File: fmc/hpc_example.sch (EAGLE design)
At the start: 4 parts

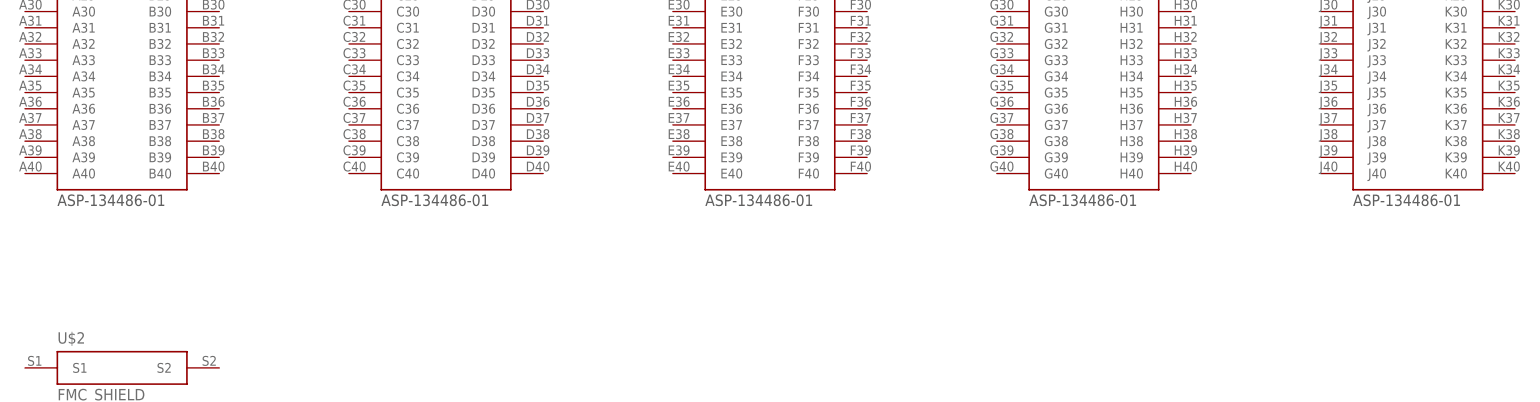
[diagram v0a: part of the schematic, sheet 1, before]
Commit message: added fmc lpc connector
updated naming
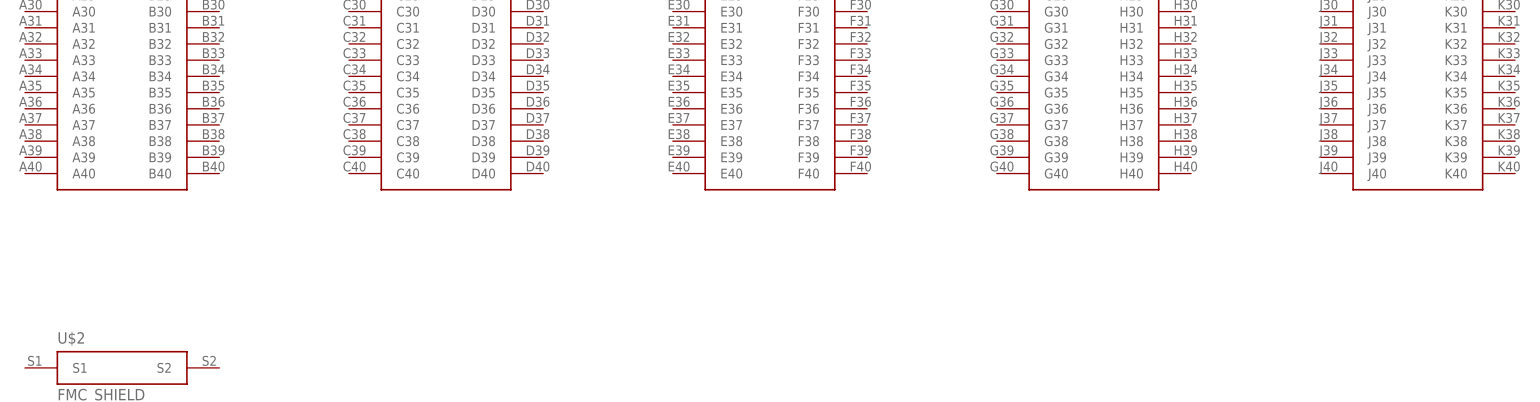
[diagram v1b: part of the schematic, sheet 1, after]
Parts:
- U$1: value FMC_HPC_M -> APS_HPC_M; device flipbit_fmc:FMC_HPC_M -> flipbit_fmc:APS_HPC_M
- U$3: value FMC_HPC_F -> APS_HPC_F; device flipbit_fmc:FMC_HPC_F -> flipbit_fmc:APS_HPC_F
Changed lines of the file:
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@@
 </classes>
 <parts>
-<part name="U$1" library="flipbit_fmc" deviceset="FMC_HPC_M" device=""/>
+<part name="U$1" library="flipbit_fmc" deviceset="APS_HPC_M" device=""/>
 <part name="U$2" library="flipbit_fmc" deviceset="XILINX_FMC_MOUNT_CS" device=""/>
-<part name="U$3" library="flipbit_fmc" deviceset="FMC_HPC_F" device=""/>
+<part name="U$3" library="flipbit_fmc" deviceset="APS_HPC_F" device=""/>
 <part name="U$4" library="flipbit_fmc" deviceset="XILINX_FMC_MOUNT_BS" device=""/>
 <part name="FRAME1" library="frames" deviceset="DINA4_L" device=""/>
